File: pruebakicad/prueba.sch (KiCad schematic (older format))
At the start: 2 parts

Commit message: pins
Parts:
- added U?: TLV1117-33, symbol Regulator_Linear:TLV1117-33
- added U?: TLV1117-50, symbol Regulator_Linear:TLV1117-50
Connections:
- net GND: now also U?.1 (GND), U?.1 (GND)
- new net +12V: U?.3 (VI), U?.3 (VI)
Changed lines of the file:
@@
 F0 "esp32-wroom" 20
 F1 "esp.sch" 20
+F2 "SDA" I R 4150 1900 50
+F3 "SCL" I R 4150 2000 50
+F4 "SCK" I R 4150 2100 50
+F5 "MISO" I R 4150 2200 50
+F6 "RST" I R 4150 2300 50
+F7 "MOSI" I R 4150 2400 50
 $EndSheet
 $Comp
@@
 SDA
 $Comp
-L power:+5V #PWR?
-U 1 1 6079ADA1
-P 5250 3000
-F 0 "#PWR?" H 5250 2850 50  0001 C CNN
-F 1 "+5V" H 5265 3173 50  0000 C CNN
-F 2 "" H 5250 3000 50  0001 C CNN
-F 3 "" H 5250 3000 50  0001 C CNN
-	1    5250 3000
-	1    0    0    -1
-$EndComp
-$Comp
 L power:GND #PWR?
 U 1 1 6079B324
@@
 Wire Wire Line
 	5250 3400 5250 3550
+$Comp
+L Regulator_Linear:TLV1117-33 U?
+U 1 1 60787907
+P 1500 1850
+F 0 "U?" H 1500 2092 50  0000 C CNN
+F 1 "TLV1117-33" H 1500 2001 50  0000 C CNN
+F 2 "" H 1500 1850 50  0001 C CNN
+F 3 "http://www.ti.com/lit/ds/symlink/tlv1117.pdf" H 1500 1850 50  0001 C CNN
+	1    1500 1850
+	1    0    0    -1
+$EndComp
+$Comp
+L Regulator_Linear:TLV1117-50 U?
+U 1 1 60788435
+P 1550 3050
+F 0 "U?" H 1550 3292 50  0000 C CNN
+F 1 "TLV1117-50" H 1550 3201 50  0000 C CNN
+F 2 "" H 1550 3050 50  0001 C CNN
+F 3 "http://www.ti.com/lit/ds/symlink/tlv1117.pdf" H 1550 3050 50  0001 C CNN
+	1    1550 3050
+	1    0    0    -1
+$EndComp
+$Comp
+L power:+12V #PWR?
+U 1 1 6078B4F0
+P 1100 1800
+F 0 "#PWR?" H 1100 1650 50  0001 C CNN
+F 1 "+12V" H 1115 1973 50  0000 C CNN
+F 2 "" H 1100 1800 50  0001 C CNN
+F 3 "" H 1100 1800 50  0001 C CNN
+	1    1100 1800
+	1    0    0    -1
+$EndComp
+$Comp
+L power:+12V #PWR?
+U 1 1 6078BAF4
+P 1150 2950
+F 0 "#PWR?" H 1150 2800 50  0001 C CNN
+F 1 "+12V" H 1165 3123 50  0000 C CNN
+F 2 "" H 1150 2950 50  0001 C CNN
+F 3 "" H 1150 2950 50  0001 C CNN
+	1    1150 2950
+	1    0    0    -1
+$EndComp
+Wire Wire Line
+	1200 1850 1100 1850
+Wire Wire Line
+	1100 1850 1100 1800
+Wire Wire Line
+	1250 3050 1150 3050
+Wire Wire Line
+	1150 3050 1150 2950
+$Comp
+L power:GND #PWR?
+U 1 1 6078C8AB
+P 1550 3500
+F 0 "#PWR?" H 1550 3250 50  0001 C CNN
+F 1 "GND" H 1555 3327 50  0000 C CNN
+F 2 "" H 1550 3500 50  0001 C CNN
+F 3 "" H 1550 3500 50  0001 C CNN
+	1    1550 3500
+	1    0    0    -1
+$EndComp
+$Comp
+L power:GND #PWR?
+U 1 1 6078CE90
+P 1500 2300
+F 0 "#PWR?" H 1500 2050 50  0001 C CNN
+F 1 "GND" H 1505 2127 50  0000 C CNN
+F 2 "" H 1500 2300 50  0001 C CNN
+F 3 "" H 1500 2300 50  0001 C CNN
+	1    1500 2300
+	1    0    0    -1
+$EndComp
+Wire Wire Line
+	1500 2150 1500 2300
+Wire Wire Line
+	1550 3350 1550 3500
+$Comp
+L power:+5V #PWR?
+U 1 1 6079ADA1
+P 5250 3000
+F 0 "#PWR?" H 5250 2850 50  0001 C CNN
+F 1 "+5V" H 5265 3173 50  0000 C CNN
+F 2 "" H 5250 3000 50  0001 C CNN
+F 3 "" H 5250 3000 50  0001 C CNN
+	1    5250 3000
+	1    0    0    -1
+$EndComp
 $EndSCHEMATC

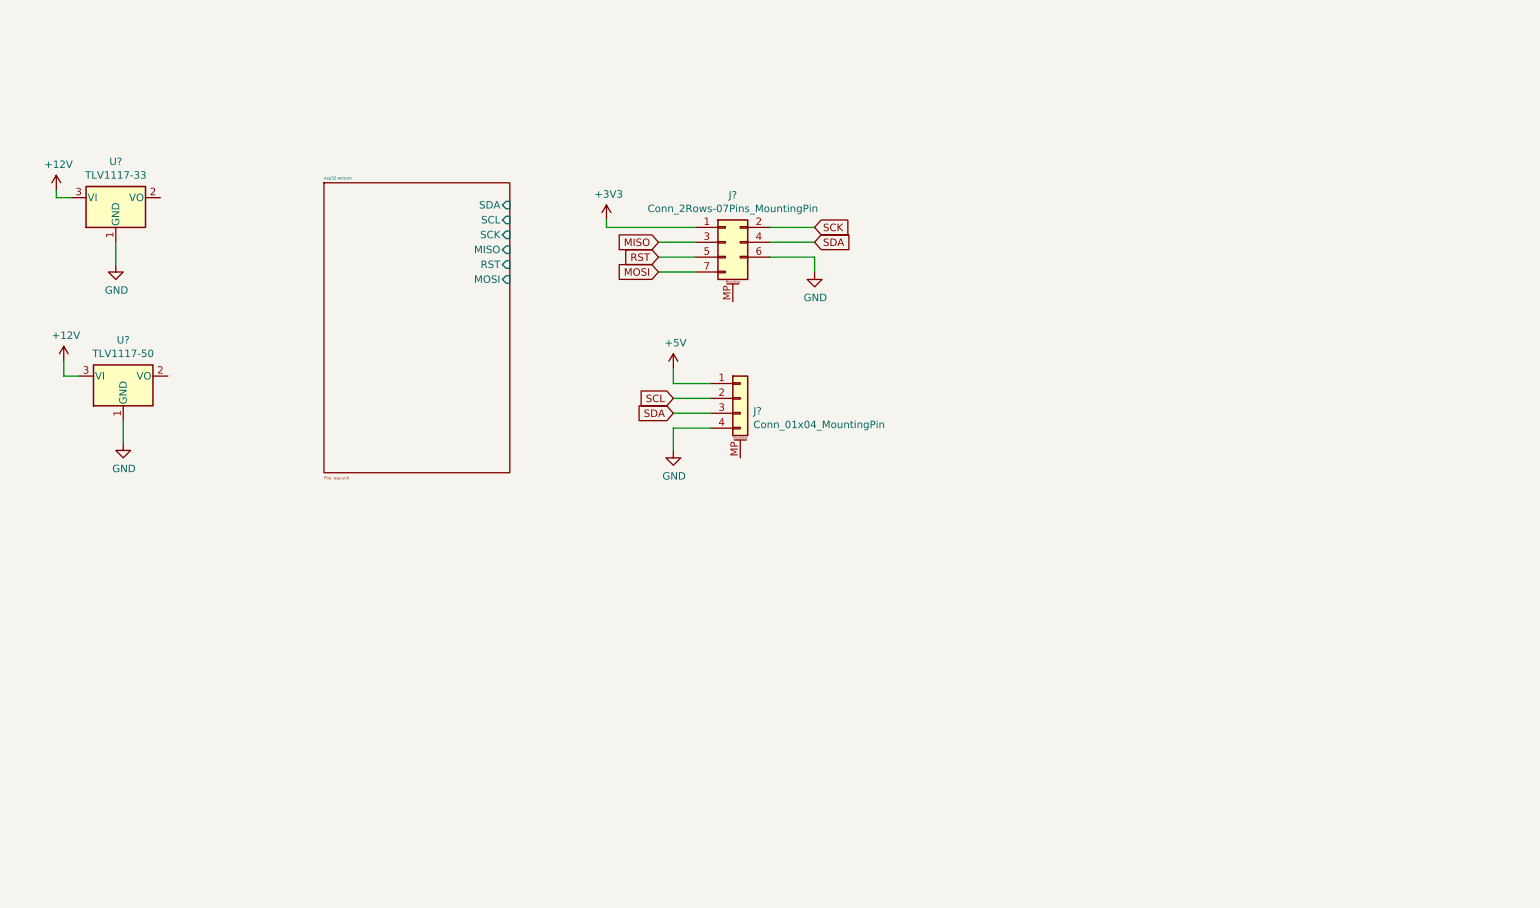
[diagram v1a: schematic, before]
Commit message: More peripherals
Added some peripherals and last ones were fixed
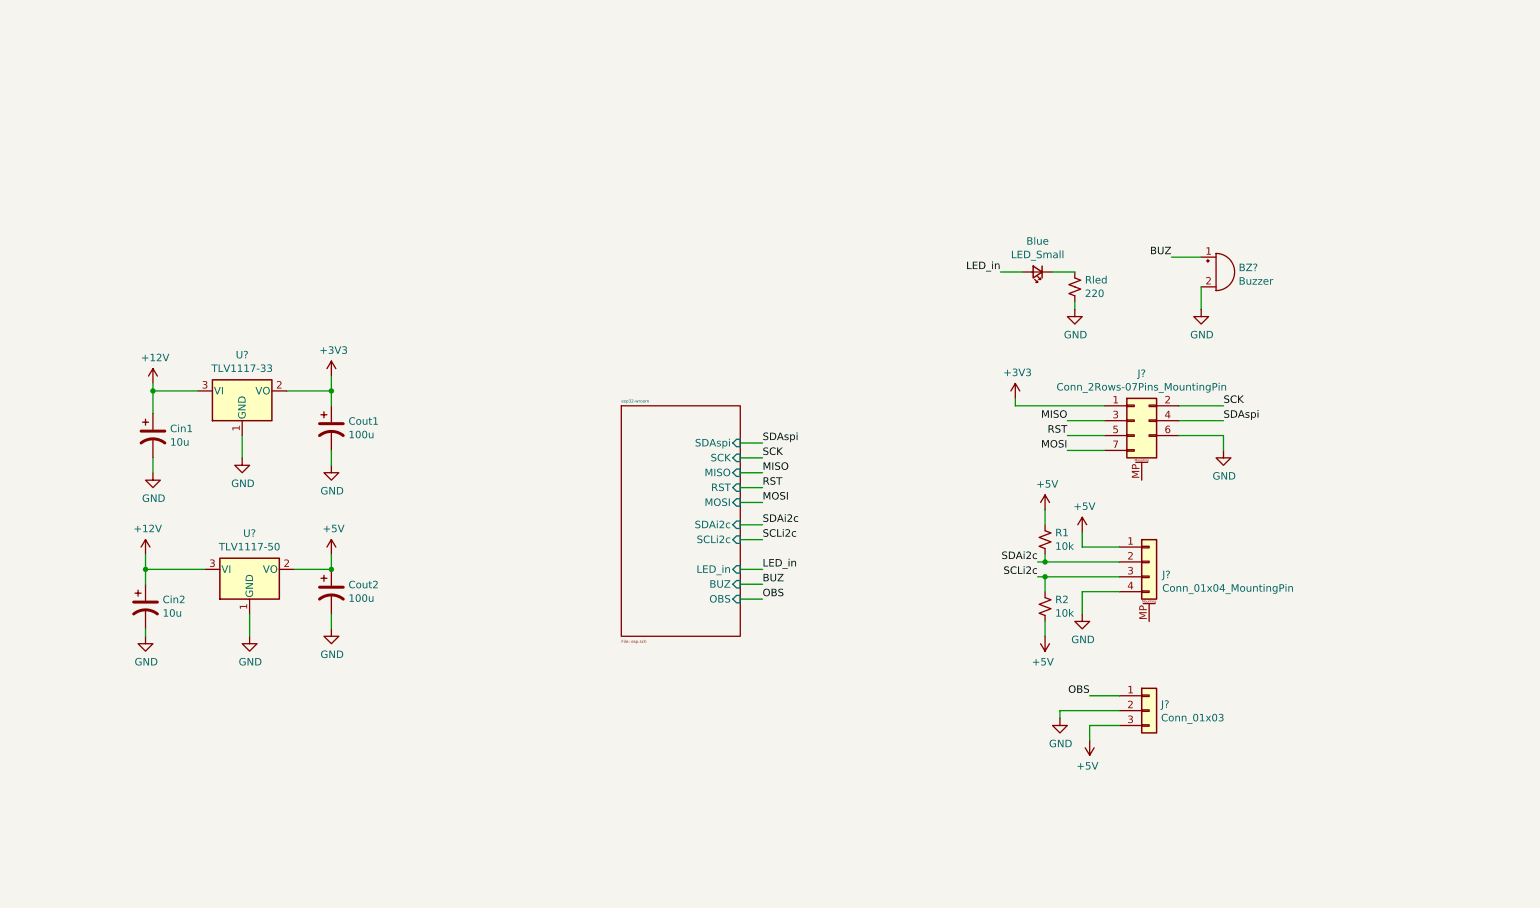
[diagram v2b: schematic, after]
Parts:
- added BZ?: Buzzer, symbol Device:Buzzer
- added Blue: LED_Small, symbol Device:LED_Small
- added Cin1, Cin2: 10u, symbol Device:CP1
- added Cout1, Cout2: 100u, symbol Device:CP1
- added J?: Conn_01x03, symbol Connector_Generic:Conn_01x03
- added R1, R2: 10k, symbol Device:R_Small_US
- added Rled: 220, symbol Device:R_Small_US
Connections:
- net +12V: now also Cin1.1, Cin2.1
- net +3V3: now also U?.2 (VO), Cout1.1
- net +5V: now also U?.2 (VO), Cout2.1, J?.3 (Pin_3), R1.1, R2.2
- net GND: now also BZ?.2 (+), Cin1.2, Cin2.2, Cout1.2, Cout2.2, J?.2 (Pin_2), Rled.1
- net SCL renamed SDAi2c
- net SDAi2c: now also R1.2
- net SDA renamed SCLi2c
- net SCLi2c: now also R2.1; no longer J?.4 (Pin_4)
- new net: Blue.1 (K), Rled.2
- new net BUZ: BZ?.1 (-)
- new net LED_in: Blue.2 (A)
- new net OBS: J?.1 (Pin_1)
- new net SDAspi: J?.4 (Pin_4)
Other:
- moved on the sheet: J?, U?

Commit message: Added_gpios
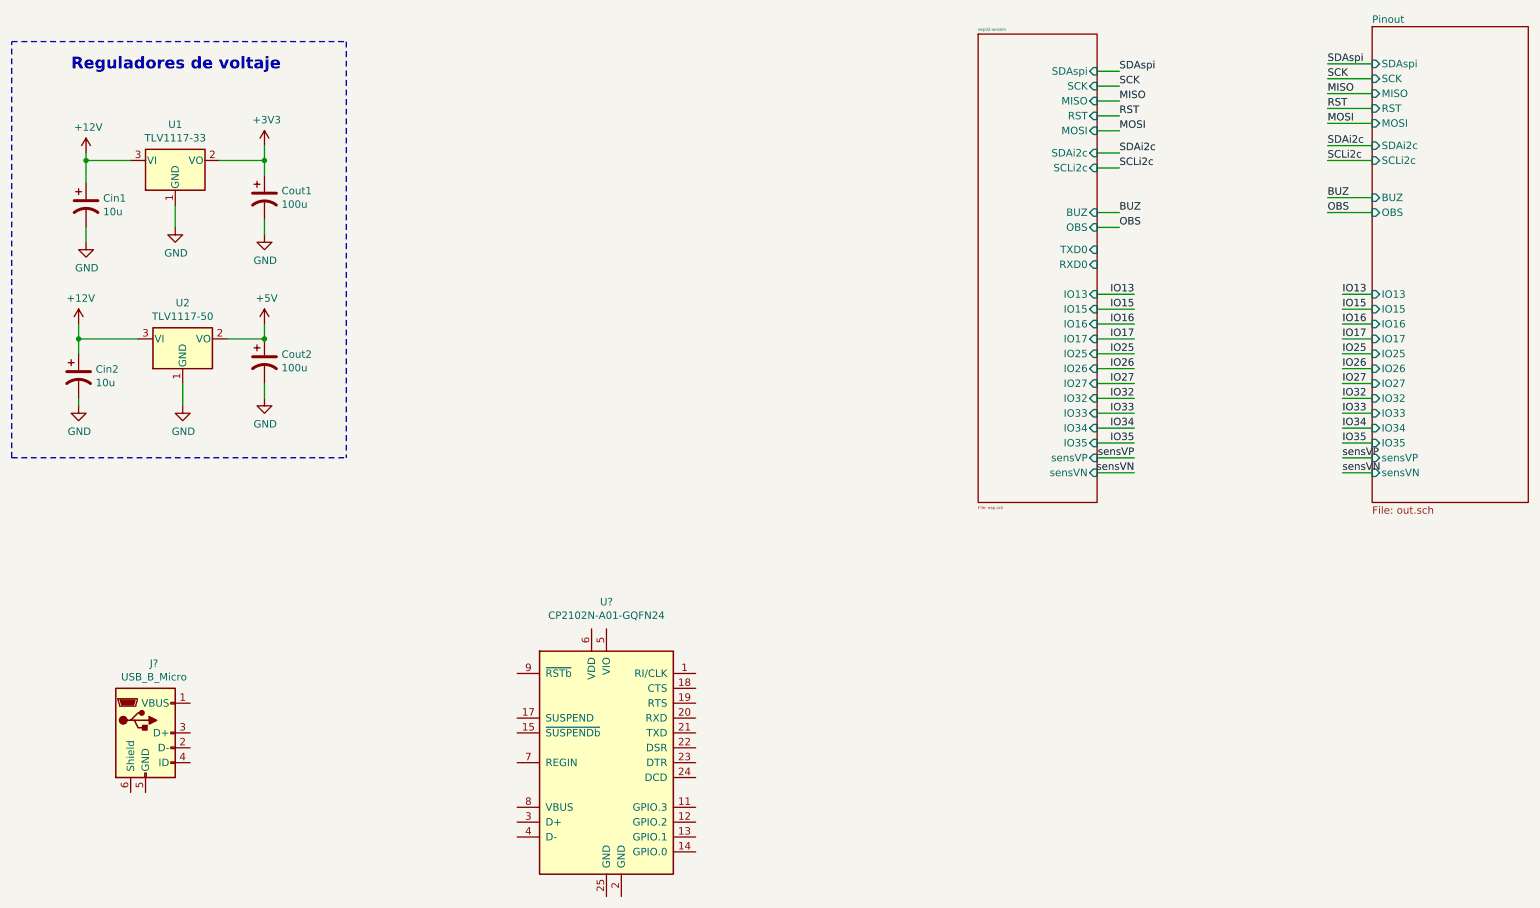
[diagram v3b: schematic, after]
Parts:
- removed BZ?: Buzzer, symbol Device:Buzzer
- removed Blue: LED_Small, symbol Device:LED_Small
- removed J?: Conn_2Rows-07Pins_MountingPin, symbol Connector_Generic_MountingPin:Conn_2Rows-07Pins_MountingPin
- removed J?: Conn_01x04_MountingPin, symbol Connector_Generic_MountingPin:Conn_01x04_MountingPin
- removed J?: Conn_01x03, symbol Connector_Generic:Conn_01x03
- removed R1, R2: 10k, symbol Device:R_Small_US
- removed Rled: 220, symbol Device:R_Small_US
- added J?: USB_B_Micro, symbol Connector:USB_B_Micro
- added U?: CP2102N-A01-GQFN24, Package_DFN_QFN:QFN-24-1EP_4x4mm_P0.5mm_EP2.6x2.6mm, symbol Interface_USB:CP2102N-A01-GQFN24
- gave numbers to parts that had none: 2
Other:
- note added: "Reguladores de voltaje"
- moved on the sheet: Cin1, Cin2, Cout1, Cout2, U1, U2

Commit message: uart_added
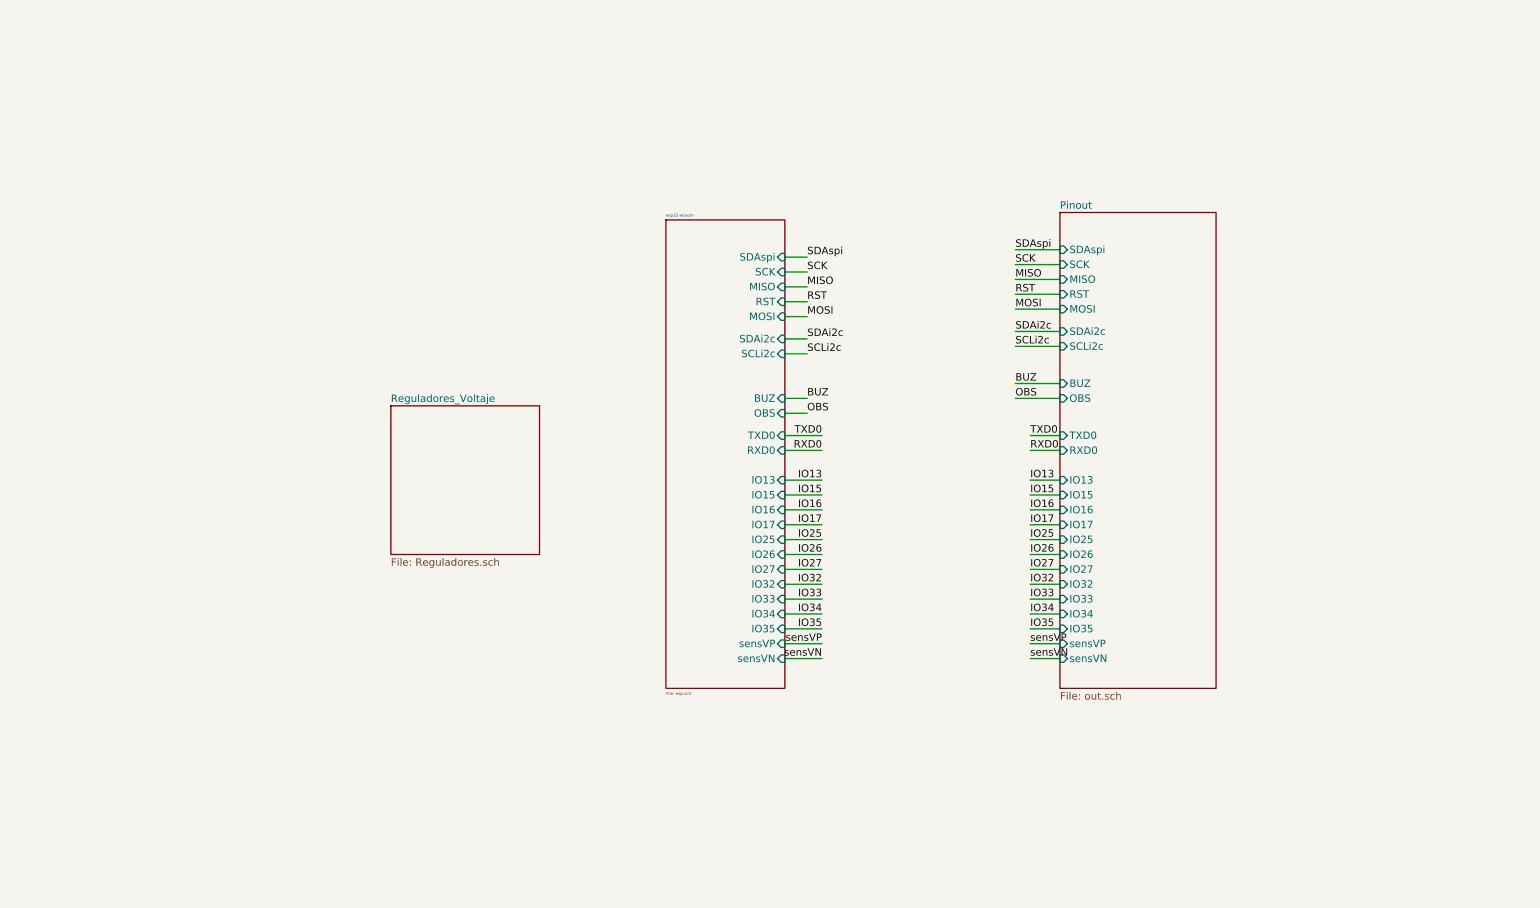
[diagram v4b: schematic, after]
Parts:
- removed Cin1, Cin2: 10u, symbol Device:CP1
- removed Cout1, Cout2: 100u, symbol Device:CP1
- removed J?: USB_B_Micro, symbol Connector:USB_B_Micro
- removed U1: TLV1117-33, symbol Regulator_Linear:TLV1117-33
- removed U2: TLV1117-50, symbol Regulator_Linear:TLV1117-50
- removed U?: CP2102N-A01-GQFN24, Package_DFN_QFN:QFN-24-1EP_4x4mm_P0.5mm_EP2.6x2.6mm, symbol Interface_USB:CP2102N-A01-GQFN24
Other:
- note removed: "Reguladores de voltaje"
